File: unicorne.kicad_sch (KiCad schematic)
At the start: 22 parts, among them J1 Battery, J2 TPS43, J3 Expansion, J4 GPIO, J5 PAW3395 / PMW3360, J6 LED power in, Q1 AO3401A, Q2 2N7002, SW43 Power, SW44 Reset, U1 nice!nano v2, U2 SN74LV1T125

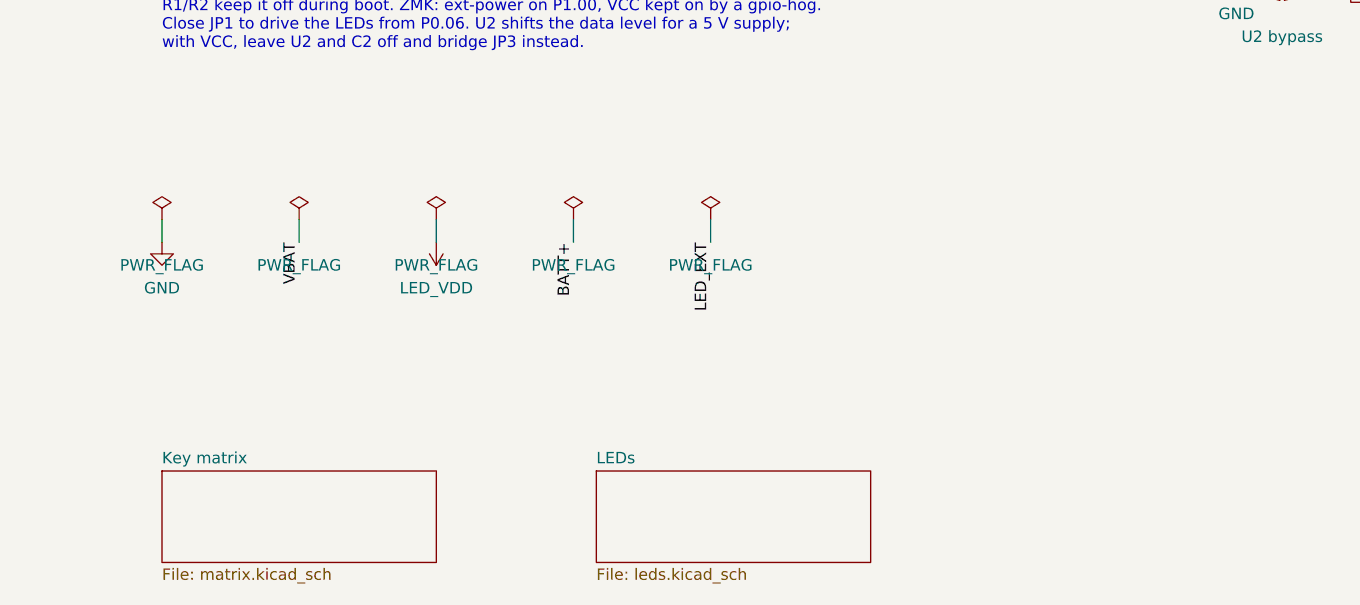
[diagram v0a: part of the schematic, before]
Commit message: Route both boards with KiCadRoutingTools; no vias in pads
tools/krt_route.py: fixed lanes, then KiCadRoutingTools 0.23.7 for every other
signal at standard JLCPCB sizes (0.6/0.3 vias, 0.2 tracks) with no via in or next
to a pad, own net's included; the maze router for any net it could only finish
with undersized vias; GND pours and stitching; its plane repair; then any via
touching a pad is removed. The tools relax the project's rules on disk: ours are
put back.

MX lanes: LED_VDD's jog across a break line moves from 5.5 to 4.5 mm off the
line. At 5.5 it boxed in the outer-column LED DIN pads, so 8 LED data links had
no room for a via outside a pad. Lane-only board: no DRC errors.

Stitching vias (finish_route.stitch) and our maze router stay off SMD pads too.
The previous MX board had 82 vias in pads, now none on either board.

MX: U2 pad 3 (GND) is boxed in by LED_DIN; joined by hand with a via between
pads 3 and 4 (noted in the README).

Both boards: DRC 0 unconnected, 0 copper violations, schematic parity clean;
all 482 schematic pins, 42 keys and the 54-LED chain check out pin by pin.
Waves, LED map, plates, gerbers, STEP and renders regenerated.

Co-Authored-By: Claude Opus 5.5 <noreply@anthropic.com>
Claude-Session: https://claude.ai/code/session_01D39ubfTYtq6FMvNmmbStTo
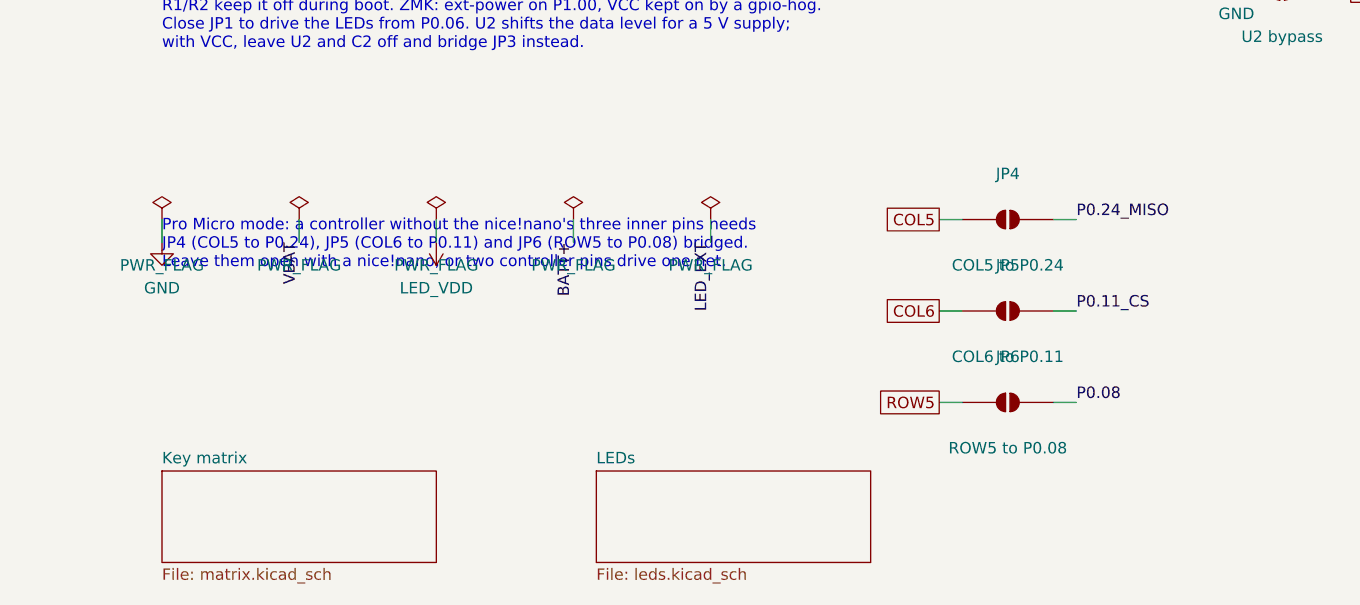
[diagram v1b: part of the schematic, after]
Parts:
- added JP4: COL5 to P0.24, Jumper:SolderJumper-2_P1.3mm_Open_RoundedPad1.0x1.5mm, symbol Jumper:SolderJumper_2_Open
- added JP5: COL6 to P0.11, Jumper:SolderJumper-2_P1.3mm_Open_RoundedPad1.0x1.5mm, symbol Jumper:SolderJumper_2_Open
- added JP6: ROW5 to P0.08, Jumper:SolderJumper-2_P1.3mm_Open_RoundedPad1.0x1.5mm, symbol Jumper:SolderJumper_2_Open
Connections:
- net COL5: now also JP4.1 (A)
- net COL6: now also JP5.1 (A)
- net P0.08: now also JP6.2 (B)
- net P0.11_CS: now also JP5.2 (B)
- net P0.24_MISO: now also JP4.2 (B)
- net ROW5: now also JP6.1 (A)
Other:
- note added: "Pro Micro mode: a controller without the nice!nano's three inner pins needs JP4 (COL5 to P0.24), JP5 (COL6 to P0.11) and JP6 (ROW5 to P0.08) bridged. Leave them open with a nice!nano, or two controller pins drive one net."
